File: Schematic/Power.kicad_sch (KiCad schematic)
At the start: 42 parts, among them IC1 MP9943AGQ-Z, IC2 MP9943AGQ-Z, U2 ME6217C33M5G, U3 LDO-1.8v

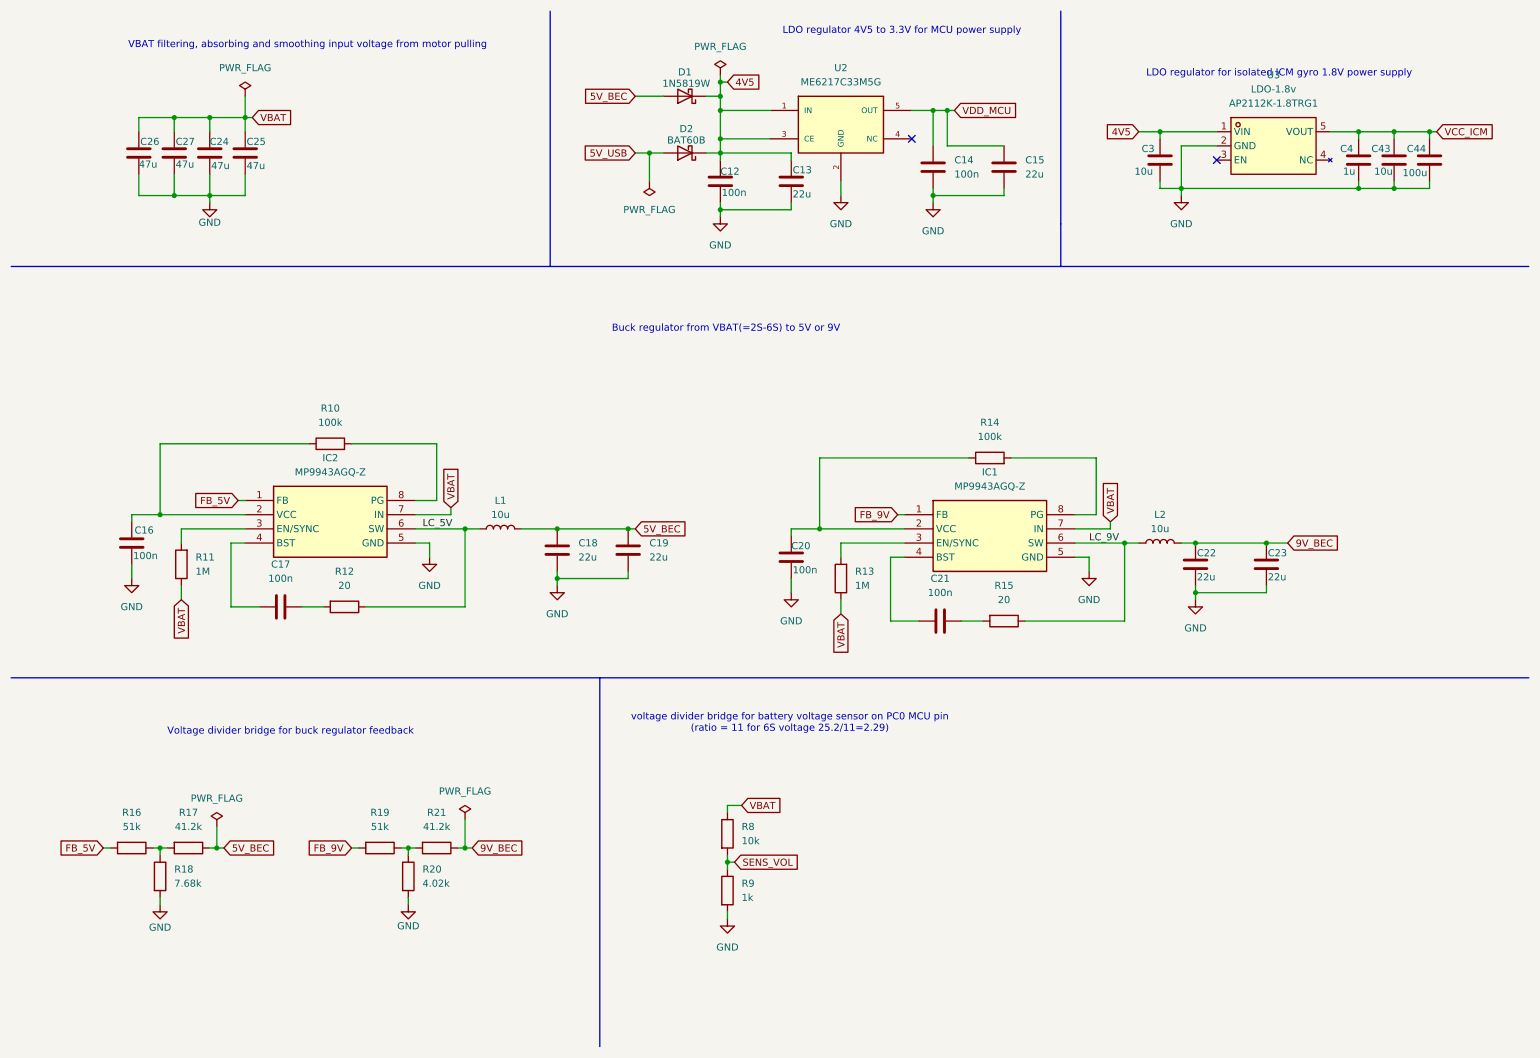
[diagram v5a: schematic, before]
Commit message: update schematic after reviewing some footprints
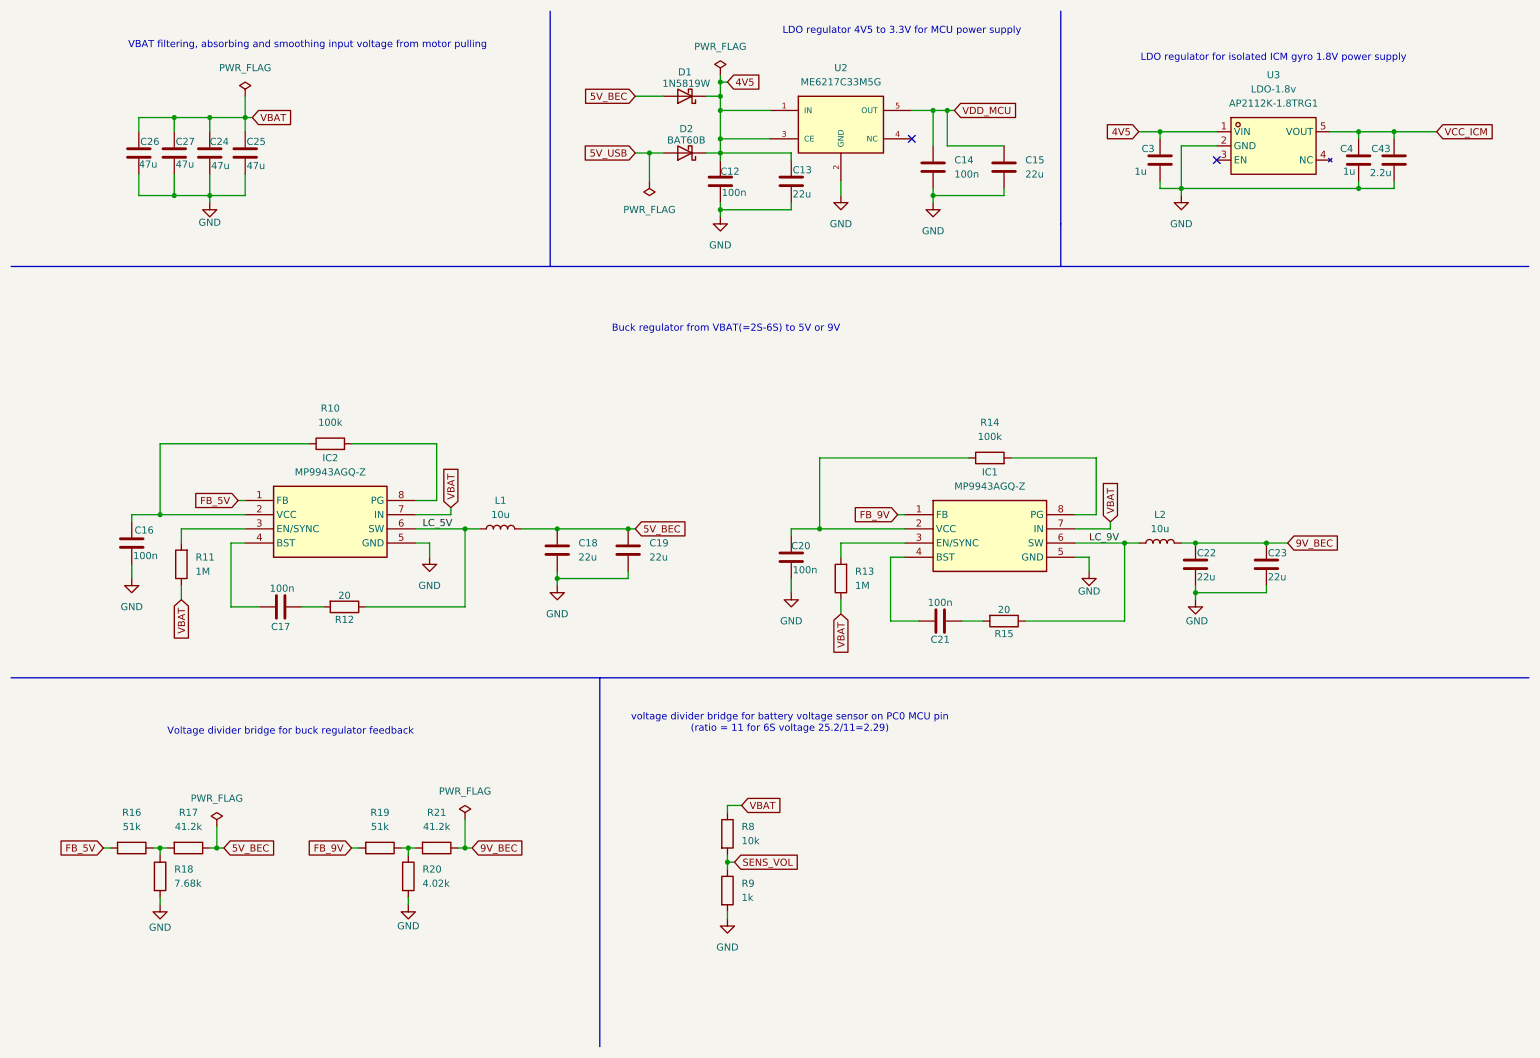
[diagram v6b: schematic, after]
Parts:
- removed C44: 100u, Capacitor_SMD:C_0805_2012Metric, symbol Device:C
- C12, C14, C16, C17, C20, C21: MPN 0603B104K500NT -> (none); Manufacturer FH -> (none)
- C3: value 10u -> 1u; footprint Capacitor_SMD:C_0805_2012Metric -> Capacitor_SMD:C_0603_1608Metric; MPN CL21A226MAQNNNE -> CL10A105KB8NNNC
- C4: footprint Capacitor_SMD:C_0805_2012Metric -> Capacitor_SMD:C_0603_1608Metric; MPN CL21A226MAQNNNE -> CL10A105KB8NNNC
- C43: value 10u -> 2.2u; footprint Capacitor_SMD:C_0805_2012Metric -> Capacitor_SMD:C_0603_1608Metric; MPN CL21A226MAQNNNE -> (none); Manufacturer SAMSUNG -> (none)
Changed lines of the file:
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@@
 	(text "LDO regulator for isolated ICM gyro 1.8V power supply"
 		(exclude_from_sim no)
-		(at 239.776 23.876 0)
+		(at 238.76 21.082 0)
 		(effects
 			(font
@@
 	)
 	(junction
-		(at 260.35 44.45)
-		(diameter 0)
-		(color 0 0 0 0)
-	)
-	(junction
 		(at 177.8 45.72)
 		(diameter 0)
@@
 	)
 	(junction
-		(at 266.7 34.29)
-		(diameter 0)
-		(color 0 0 0 0)
-	)
-	(junction
 		(at 48.26 31.75)
 		(diameter 0)
@@
 	(wire
 		(pts
-			(xy 266.7 34.29) (xy 267.97 34.29)
-		)
-		(stroke
-			(width 0)
-			(type default)
-		)
-	)
-	(wire
-		(pts
 			(xy 34.29 102.87) (xy 34.29 104.14)
 		)
@@
 	(wire
 		(pts
-			(xy 266.7 43.18) (xy 266.7 44.45)
-		)
-		(stroke
-			(width 0)
-			(type default)
-		)
-	)
-	(wire
-		(pts
 			(xy 73.66 90.17) (xy 88.9 90.17)
 		)
@@
 	(wire
 		(pts
-			(xy 266.7 34.29) (xy 266.7 35.56)
-		)
-		(stroke
-			(width 0)
-			(type default)
-		)
-	)
-	(wire
-		(pts
 			(xy 237.49 107.95) (xy 241.3 107.95)
 		)
@@
 	(wire
 		(pts
-			(xy 260.35 34.29) (xy 266.7 34.29)
+			(xy 260.35 34.29) (xy 267.97 34.29)
 		)
 		(stroke
@@
 	(wire
 		(pts
-			(xy 266.7 44.45) (xy 260.35 44.45)
-		)
-		(stroke
-			(width 0)
-			(type default)
-		)
-	)
-	(wire
-		(pts
 			(xy 83.82 162.56) (xy 83.82 163.83)
 		)
@@
 			)
 		)
-		(property "Footprint" "Capacitor_SMD:C_0805_2012Metric"
+		(property "Footprint" "Capacitor_SMD:C_0603_1608Metric"
 			(at 254.9652 43.18 0)
 			(effects
@@
 			)
 		)
-		(property "MPN" "CL21A226MAQNNNE"
+		(property "MPN" "CL10A105KB8NNNC"
 			(at 254 39.37 0)
 			(effects
@@
 			)
 		)
-		(property "Value" "10u"
+		(property "Value" "1u"
 			(at 213.868 41.402 0)
 			(effects
@@
 			)
 		)
-		(property "Footprint" "Capacitor_SMD:C_0805_2012Metric"
+		(property "Footprint" "Capacitor_SMD:C_0603_1608Metric"
 			(at 219.4052 43.18 0)
 			(effects
@@
 			)
 		)
-		(property "MPN" "CL21A226MAQNNNE"
+		(property "MPN" "CL10A105KB8NNNC"
 			(at 218.44 39.37 0)
 			(effects
@@
 			)
 		)
-		(property "Datasheet" "https://www.lcsc.com/datasheet/C30926.pdf"
+		(property "Datasheet" ""
 			(at 177.8 40.64 0)
 			(effects
@@
 			)
 		)
-		(property "MPN" "0603B104K500NT "
+		(property "MPN" ""
 			(at 177.8 40.64 0)
 			(effects
@@
 			)
 		)
-		(property "Manufacturer" "FH"
+		(property "Manufacturer" ""
 			(at 177.8 40.64 0)
 			(effects
@@
 		(on_board yes)
 		(dnp no)
-		(fields_autoplaced yes)
 		(property "Reference" "R15"
-			(at 190.5 115.57 90)
+			(at 190.5 124.206 90)
 			(effects
 				(font
@@
 		)
 		(property "Value" "20"
-			(at 190.5 118.11 90)
+			(at 190.5 119.888 90)
 			(effects
 				(font
@@
 		(on_board yes)
 		(dnp no)
-		(fields_autoplaced yes)
 		(property "Reference" "R12"
-			(at 72.39 113.03 90)
+			(at 72.39 121.666 90)
 			(effects
 				(font
@@
 		)
 		(property "Value" "20"
-			(at 72.39 115.57 90)
+			(at 72.39 117.348 90)
 			(effects
 				(font
@@
 		(on_board yes)
 		(dnp no)
-		(fields_autoplaced yes)
 		(property "Reference" "C21"
-			(at 179.07 114.3 90)
+			(at 179.07 125.222 90)
 			(effects
 				(font
@@
 		)
 		(property "Value" "100n"
-			(at 179.07 116.84 90)
+			(at 179.07 118.618 90)
 			(effects
 				(font
@@
 			)
 		)
-		(property "Datasheet" "https://www.lcsc.com/datasheet/C30926.pdf"
+		(property "Datasheet" ""
 			(at 179.07 121.92 0)
 			(effects
@@
 			)
 		)
-		(property "MPN" "0603B104K500NT "
+		(property "MPN" ""
 			(at 179.07 121.92 90)
 			(effects
@@
 			)
 		)
-		(property "Manufacturer" "FH"
+		(property "Manufacturer" ""
 			(at 179.07 121.92 90)
 			(effects
@@
 			)
 		)
-		(property "Value" "10u"
-			(at 256.794 41.402 0)
+		(property "Value" "2.2u"
+			(at 256.032 41.656 0)
 			(effects
 				(font
@@
 			)
 		)
-		(property "Footprint" "Capacitor_SMD:C_0805_2012Metric"
+		(property "Footprint" "Capacitor_SMD:C_0603_1608Metric"
 			(at 261.3152 43.18 0)
 			(effects
@@
 			)
 		)
-		(property "Datasheet" "https://www.samsungsem.com/resources/file/global/support/product_catalog/MLCC.pdf"
+		(property "Datasheet" ""
 			(at 260.35 39.37 0)
 			(effects
@@
 			)
 		)
-		(property "MPN" "CL21A226MAQNNNE"
+		(property "MPN" ""
 			(at 260.35 39.37 0)
 			(effects
@@
 			)
 		)
-		(property "Manufacturer" "SAMSUNG"
+		(property "Manufacturer" ""
 			(at 260.35 39.37 0)
 			(effects
@@
 		(on_board yes)
 		(dnp no)
-		(fields_autoplaced yes)
 		(property "Reference" "#PWR017"
 			(at 224.79 124.46 0)
@@
 		)
 		(property "Value" "GND"
-			(at 224.79 123.19 0)
+			(at 225.044 121.92 0)
 			(effects
 				(font
@@
 			)
 		)
-		(property "Datasheet" "https://www.lcsc.com/datasheet/C30926.pdf"
+		(property "Datasheet" ""
 			(at 139.7 43.18 0)
 			(effects
@@
 			)
 		)
-		(property "MPN" "0603B104K500NT "
+		(property "MPN" ""
 			(at 139.7 43.18 0)
 			(effects
@@
 			)
 		)
-		(property "Manufacturer" "FH"
+		(property "Manufacturer" ""
 			(at 139.7 43.18 0)
 			(effects
@@
 		(on_board yes)
 		(dnp no)
-		(fields_autoplaced yes)
 		(property "Reference" "#PWR016"
 			(at 205.74 119.38 0)
@@
 		)
 		(property "Value" "GND"
-			(at 205.74 118.11 0)
+			(at 205.74 116.586 0)
 			(effects
 				(font
@@
 			)
 		)
-		(property "Datasheet" "https://www.lcsc.com/datasheet/C30926.pdf"
+		(property "Datasheet" ""
 			(at 152.4 110.49 0)
 			(effects
@@
 			)
 		)
-		(property "MPN" "0603B104K500NT "
+		(property "MPN" ""
 			(at 152.4 110.49 90)
 			(effects
@@
 			)
 		)
-		(property "Manufacturer" "FH"
+		(property "Manufacturer" ""
 			(at 152.4 110.49 90)
 			(effects
@@
 		(on_board yes)
 		(dnp no)
-		(fields_autoplaced yes)
 		(property "Reference" "C17"
-			(at 60.96 111.76 90)
+			(at 60.96 122.936 90)
 			(effects
 				(font
@@
 		)
 		(property "Value" "100n"
-			(at 60.96 114.3 90)
+			(at 61.214 116.078 90)
 			(effects
 				(font
@@
 			)
 		)
-		(property "Datasheet" "https://www.lcsc.com/datasheet/C30926.pdf"
+		(property "Datasheet" ""
 			(at 60.96 119.38 0)
 			(effects
@@
 			)
 		)
-		(property "MPN" "0603B104K500NT "
+		(property "MPN" ""
 			(at 60.96 119.38 90)
 			(effects
@@
 			)
 		)
-		(property "Manufacturer" "FH"
+		(property "Manufacturer" ""
 			(at 60.96 119.38 90)
 			(effects
@@
 	)
 	(symbol
-		(lib_id "Device:C")
-		(at 266.7 39.37 0)
-		(unit 1)
-		(exclude_from_sim no)
-		(in_bom yes)
-		(on_board yes)
-		(dnp no)
-		(property "Reference" "C44"
-			(at 262.636 37.338 0)
-			(effects
-				(font
-					(size 1.27 1.27)
-				)
-				(justify left)
-			)
-		)
-		(property "Value" "100u"
-			(at 261.874 41.656 0)
-			(effects
-				(font
-					(size 1.27 1.27)
-				)
-				(justify left)
-			)
-		)
-		(property "Footprint" "Capacitor_SMD:C_0805_2012Metric"
-			(at 267.6652 43.18 0)
-			(effects
-				(font
-					(size 1.27 1.27)
-				)
-				(hide yes)
-			)
-		)
-		(property "Datasheet" "https://www.samsungsem.com/resources/file/global/support/product_catalog/MLCC.pdf"
-			(at 266.7 39.37 0)
-			(effects
-				(font
-					(size 1.27 1.27)
-				)
-				(hide yes)
-			)
-		)
-		(property "Description" "Unpolarized capacitor"
-			(at 266.7 39.37 0)
-			(effects
-				(font
-					(size 1.27 1.27)
-				)
-				(hide yes)
-			)
-		)
-		(property "Fréquence" ""
-			(at 266.7 39.37 0)
-			(effects
-				(font
-					(size 1.27 1.27)
-				)
-				(hide yes)
-			)
-		)
-		(property "MPN" "CL21A226MAQNNNE"
-			(at 266.7 39.37 0)
-			(effects
-				(font
-					(size 1.27 1.27)
-				)
-				(hide yes)
-			)
-		)
-		(property "Manufacturer" "SAMSUNG"
-			(at 266.7 39.37 0)
-			(effects
-				(font
-					(size 1.27 1.27)
-				)
-				(hide yes)
-			)
-		)
-		(pin "2"
-		)
-		(pin "1"
-		)
-		(instances
-			(project "fch7"
-				(path "/11716af6-0e6e-444b-b738-3f12da23c1a2/436f6237-706d-4072-be43-3abf579550aa"
-					(reference "C44")
-					(unit 1)
-				)
-			)
-		)
-	)
-	(symbol
 		(lib_id "Device:R")
 		(at 140.97 160.02 0)
@@
 			)
 		)
-		(property "Datasheet" "https://www.lcsc.com/datasheet/C30926.pdf"
+		(property "Datasheet" ""
 			(at 34.29 107.95 0)
 			(effects
@@
 			)
 		)
-		(property "MPN" "0603B104K500NT "
+		(property "MPN" ""
 			(at 34.29 107.95 90)
 			(effects
@@
 			)
 		)
-		(property "Manufacturer" "FH"
+		(property "Manufacturer" ""
 			(at 34.29 107.95 90)
 			(effects

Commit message: minor update and some checking
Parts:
- C12, C14, C16, C17, C20, C21: MPN (none) -> C0603X5R1E104K030BB; Manufacturer (none) -> TDK
- C43: MPN (none) -> 02016D225MAT2A; Manufacturer (none) -> KYOCERA AVX
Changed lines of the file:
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@@
 			)
 		)
-		(property "Datasheet" ""
+		(property "Datasheet" "https://product.tdk.com/system/files/dam/doc/product/capacitor/ceramic/mlcc/catalog/mlcc_commercial_general_en.pdf?ref_disty=mouser"
 			(at 177.8 40.64 0)
 			(effects
@@
 			)
 		)
-		(property "MPN" ""
+		(property "MPN" "C0603X5R1E104K030BB"
 			(at 177.8 40.64 0)
 			(effects
@@
 			)
 		)
-		(property "Manufacturer" ""
+		(property "Manufacturer" "TDK"
 			(at 177.8 40.64 0)
 			(effects
@@
 			)
 		)
-		(property "Datasheet" ""
+		(property "Datasheet" "https://product.tdk.com/system/files/dam/doc/product/capacitor/ceramic/mlcc/catalog/mlcc_commercial_general_en.pdf?ref_disty=mouser"
 			(at 179.07 121.92 0)
 			(effects
@@
 			)
 		)
-		(property "MPN" ""
+		(property "MPN" "C0603X5R1E104K030BB"
 			(at 179.07 121.92 90)
 			(effects
@@
 			)
 		)
-		(property "Manufacturer" ""
+		(property "Manufacturer" "TDK"
 			(at 179.07 121.92 90)
 			(effects
@@
 			)
 		)
-		(property "Datasheet" ""
+		(property "Datasheet" "https://datasheets.kyocera-avx.com/cx5r-KGM.pdf"
 			(at 260.35 39.37 0)
 			(effects
@@
 			)
 		)
-		(property "MPN" ""
+		(property "MPN" "02016D225MAT2A"
 			(at 260.35 39.37 0)
 			(effects
@@
 			)
 		)
-		(property "Manufacturer" ""
+		(property "Manufacturer" "KYOCERA AVX"
 			(at 260.35 39.37 0)
 			(effects
@@
 		(on_board yes)
 		(dnp no)
-		(fields_autoplaced yes)
 		(property "Reference" "#PWR013"
 			(at 87.63 116.84 0)
@@
 			)
 		)
-		(property "Datasheet" ""
+		(property "Datasheet" "https://product.tdk.com/system/files/dam/doc/product/capacitor/ceramic/mlcc/catalog/mlcc_commercial_general_en.pdf?ref_disty=mouser"
 			(at 139.7 43.18 0)
 			(effects
@@
 			)
 		)
-		(property "MPN" ""
+		(property "MPN" "C0603X5R1E104K030BB"
 			(at 139.7 43.18 0)
 			(effects
@@
 			)
 		)
-		(property "Manufacturer" ""
+		(property "Manufacturer" "TDK"
 			(at 139.7 43.18 0)
 			(effects
@@
 			)
 		)
-		(property "Datasheet" ""
+		(property "Datasheet" "https://product.tdk.com/system/files/dam/doc/product/capacitor/ceramic/mlcc/catalog/mlcc_commercial_general_en.pdf?ref_disty=mouser"
 			(at 152.4 110.49 0)
 			(effects
@@
 			)
 		)
-		(property "MPN" ""
+		(property "MPN" "C0603X5R1E104K030BB"
 			(at 152.4 110.49 90)
 			(effects
@@
 			)
 		)
-		(property "Manufacturer" ""
+		(property "Manufacturer" "TDK"
 			(at 152.4 110.49 90)
 			(effects
@@
 			)
 		)
-		(property "Datasheet" ""
+		(property "Datasheet" "https://product.tdk.com/system/files/dam/doc/product/capacitor/ceramic/mlcc/catalog/mlcc_commercial_general_en.pdf?ref_disty=mouser"
 			(at 60.96 119.38 0)
 			(effects
@@
 			)
 		)
-		(property "MPN" ""
+		(property "MPN" "C0603X5R1E104K030BB"
 			(at 60.96 119.38 90)
 			(effects
@@
 			)
 		)
-		(property "Manufacturer" ""
+		(property "Manufacturer" "TDK"
 			(at 60.96 119.38 90)
 			(effects
@@
 			)
 		)
-		(property "Datasheet" ""
+		(property "Datasheet" "https://product.tdk.com/system/files/dam/doc/product/capacitor/ceramic/mlcc/catalog/mlcc_commercial_general_en.pdf?ref_disty=mouser"
 			(at 34.29 107.95 0)
 			(effects
@@
 			)
 		)
-		(property "MPN" ""
+		(property "MPN" "C0603X5R1E104K030BB"
 			(at 34.29 107.95 90)
 			(effects
@@
 			)
 		)
-		(property "Manufacturer" ""
+		(property "Manufacturer" "TDK"
 			(at 34.29 107.95 90)
 			(effects
